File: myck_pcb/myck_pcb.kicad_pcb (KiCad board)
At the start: 2 copper layers, 20 x 78 mm, 8 parts, among them T1 SW_Push_45deg

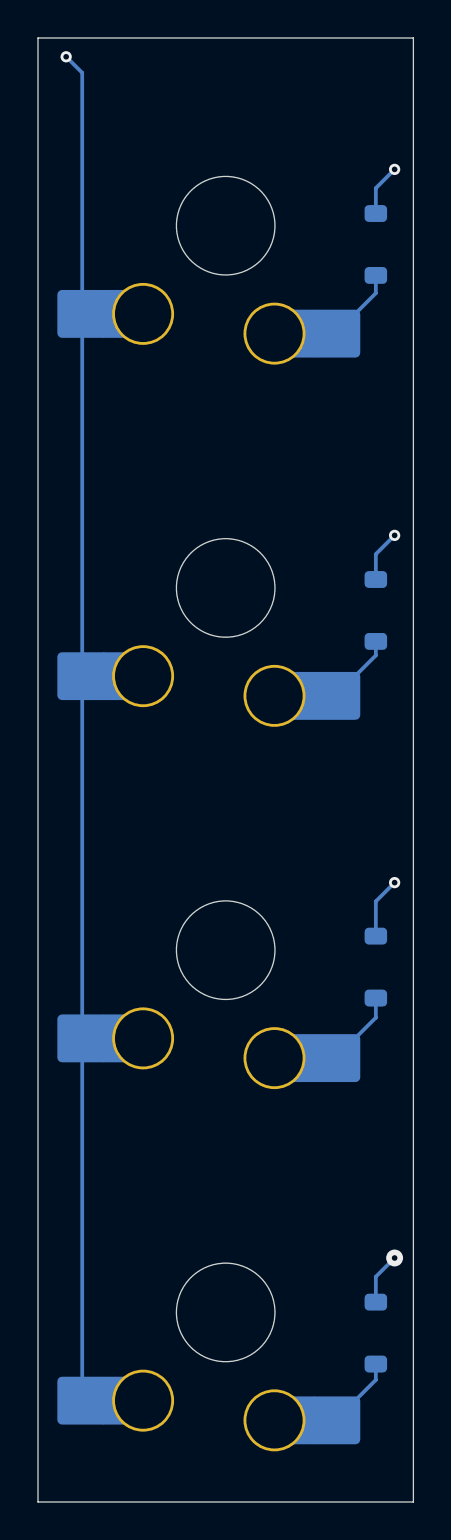
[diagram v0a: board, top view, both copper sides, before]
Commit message: Añadidos Leds, circuitos y pines
En principio, creo que ya estaría la circuitería hecha.
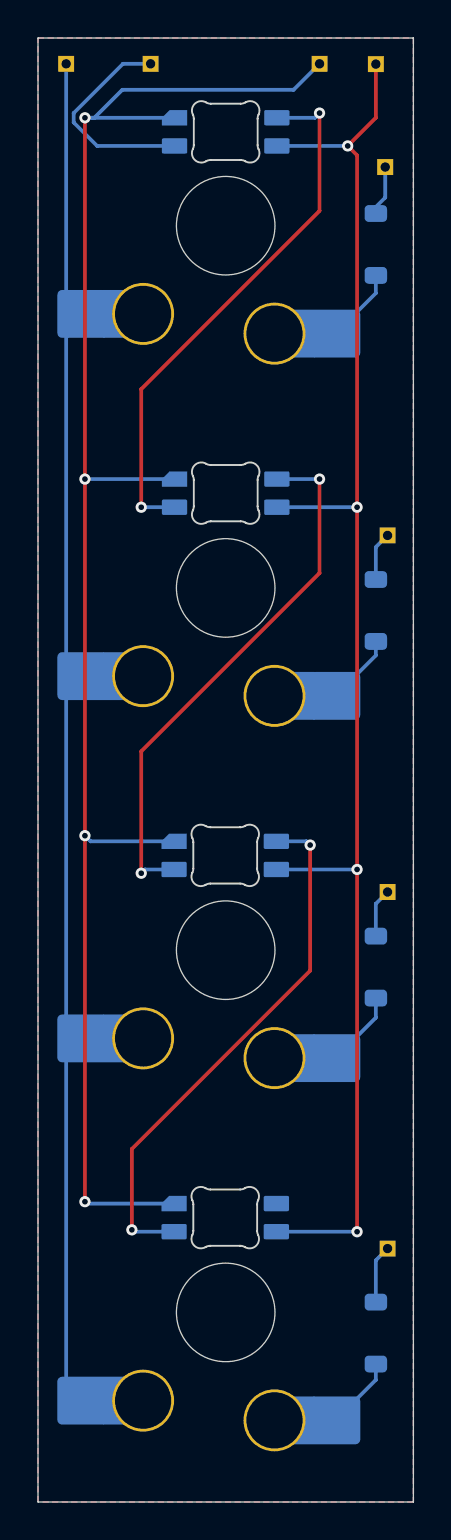
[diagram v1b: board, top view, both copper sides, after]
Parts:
- added 5V: PinHeader_1x01_P1.00mm_Horizontal, Connector_PinHeader_1.00mm:PinHeader_1x01_P1.00mm_Horizontal, B.Cu at (117.5, 70.9)
- added COL: PinHeader_1x01_P1.00mm_Horizontal, Connector_PinHeader_1.00mm:PinHeader_1x01_P1.00mm_Horizontal, B.Cu at (101.0, 70.9)
- added GND: PinHeader_1x01_P1.00mm_Horizontal, Connector_PinHeader_1.00mm:PinHeader_1x01_P1.00mm_Horizontal, B.Cu at (114.5, 70.9)
- added LED1: MX_SK6812MINI-E, PCM_marbastlib-mx:LED_MX_6028R, B.Cu at (109.5, 74.5)
- added LED2: MX_SK6812MINI-E, PCM_marbastlib-mx:LED_MX_6028R, B.Cu at (109.5, 93.8)
- added LED3: MX_SK6812MINI-E, PCM_marbastlib-mx:LED_MX_6028R, B.Cu at (109.5, 113.0)
- added LED4: MX_SK6812MINI-E, PCM_marbastlib-mx:LED_MX_6028R, B.Cu at (109.5, 132.3)
- added RGB: PinHeader_1x01_P1.00mm_Horizontal, Connector_PinHeader_1.00mm:PinHeader_1x01_P1.00mm_Horizontal, B.Cu at (105.5, 70.9)
- added Row0: PinHeader_1x01_P1.00mm_Horizontal, Connector_PinHeader_1.00mm:PinHeader_1x01_P1.00mm_Horizontal, B.Cu at (118.0, 76.4)
- added Row1: PinHeader_1x01_P1.00mm_Horizontal, Connector_PinHeader_1.00mm:PinHeader_1x01_P1.00mm_Horizontal, B.Cu at (118.1, 96.0)
- added Row2: PinHeader_1x01_P1.00mm_Horizontal, Connector_PinHeader_1.00mm:PinHeader_1x01_P1.00mm_Horizontal, B.Cu at (118.1, 115.0)
- added Row3: PinHeader_1x01_P1.00mm_Horizontal, Connector_PinHeader_1.00mm:PinHeader_1x01_P1.00mm_Horizontal, B.Cu at (118.1, 134.0)
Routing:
- net Earth: track 0.00 -> 90.7 mm, vias 0 -> 4
- net +5V: track 0.00 -> 79.6 mm, vias 0 -> 4
- net Net-(LED1-DOUT): track 0.00 -> 29.1 mm, vias 0 -> 2
- net Net-(LED2-DOUT): track 0.00 -> 29.0 mm, vias 0 -> 2
- net Net-(LED3-DOUT): track 0.00 -> 28.6 mm, vias 0 -> 2
- net RGB: track 0.00 -> 11.6 mm
- net Col5: track 72.0 -> 73.6 mm, vias 1 -> 0
- net unconnected-(D25-K-Pad1): track 3.26 -> 2.61 mm, vias 1 -> 0
- net unconnected-(D35-K-Pad1): track 2.76 -> 3.11 mm, vias 1 -> 0
- net unconnected-(D15-K-Pad1): track 2.76 -> 2.61 mm, vias 1 -> 0
- net unconnected-(D5-K-Pad1): track 2.76 -> 2.68 mm, vias 1 -> 0
- added copper zone on B.Cu, net Earth
- added copper zone on F.Cu, net Earth

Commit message: Movidos los footprints a directorio local
Exportados los footprints utilizados (cogidos de varias librerías de
internet) a directorio local. Así al abrir el proyecto en otro equipo,
están todos los footprints necesarios.
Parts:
- 5V, COL, GND, RGB, Row0, Row1, Row2, Row3: footprint Connector_PinHeader_1.00mm:PinHeader_1x01_P1.00mm_Horizontal -> Library:PinHeader_1x01_P1.00mm_Horizontal
- B1, G1, Space-l1, T1: footprint PCM_marbastlib-xp-gateron_lp:SW_KS33_HS_KS-2P02B01-02_HS_1u -> Library:SW_KS33_HS_KS-2P02B01-02_HS_1u
- D15, D25, D35, D5: footprint Diode_SMD:D_SOD-123 -> Library:D_SOD-123
- LED1, LED2, LED3, LED4: footprint PCM_marbastlib-mx:LED_MX_6028R -> Library:LED_MX_6028R
